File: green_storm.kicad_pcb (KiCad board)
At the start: 2 copper layers, 28 parts, among them J1 USB_B_Micro, J2 Conn_01x04, J3 Conn_01x04, J4 Conn_01x04, SW1 SW_SPDT, U1 AMS1117-3.3, U2 STM32F103C8T6, Y1 16Mhz

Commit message: Routing half-way complete
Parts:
- added H1: MountingHole, MountingHole:MountingHole_2.2mm_M2, F.Cu at (48.0, 105.0)
- added H2: MountingHole, MountingHole:MountingHole_2.2mm_M2, F.Cu at (89.9, 105.0)
- added H3: MountingHole, MountingHole:MountingHole_2.2mm_M2, F.Cu at (90.0, 80.0)
- added H4: MountingHole, MountingHole:MountingHole_2.2mm_M2, F.Cu at (48.0, 80.0)
- moved C3 98.8 mm to (64.6, 82.8)
- moved R4 91.2 mm to (64.4, 102.1), turned to 180 degrees
- moved R5 88.5 mm to (67.1, 102.1)
- moved U1 86.1 mm to (75.9, 102.7), turned to 180 degrees
- moved C1 85.5 mm to (78.4, 97.9)
- moved C2 82.5 mm to (81.5, 101.3), turned to 90 degrees
- moved J4 79.2 mm to (68.8, 110.2), turned to -90 degrees
- moved D1 78.7 mm to (84.8, 101.5), turned to 90 degrees
- moved R1 70.5 mm to (85.1, 98.3), turned to 90 degrees
- moved R2 10.3 mm to (59.8, 85.0), turned to 90 degrees
- moved J1 8.65 mm to (91.9, 89.8)
- moved SW1 7.13 mm to (44.4, 87.5), turned to -90 degrees
- moved J3 4.18 mm to (65.7, 76.1)
- moved J2 4.17 mm to (80.8, 76.1)
- moved R3 2.79 mm to (78.5, 89.4), turned to -90 degrees
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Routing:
- net Net-(J1-D-): track 0.00 -> 19.1 mm
- net Net-(J1-D+): track 0.00 -> 19.0 mm
- net Net-(J2-Pin_2): track 0.00 -> 18.4 mm
- net Net-(J3-Pin_3): track 0.00 -> 17.6 mm
- net Net-(J3-Pin_2): track 0.00 -> 17.1 mm
- net Net-(U2-BOOT0): track 0.00 -> 17.0 mm
- net +3.3V: track 0.00 -> 15.1 mm
- net GND: track 0.00 -> 14.7 mm
- net Net-(J2-Pin_3): track 0.00 -> 13.6 mm
- net Net-(U2-PD0): track 0.00 -> 8.73 mm
- net Net-(U2-PD1): track 0.00 -> 6.10 mm
- net +3.3VA: track 0.00 -> 2.13 mm
- added copper zone on B.Cu, net GND
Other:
- board outline added: 54 x 38 mm

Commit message: Power puddle dropped
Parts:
- moved R2 10.8 mm to (49.0, 84.5)
- moved J4 5.91 mm to (62.9, 110.4), turned to 90 degrees
- moved C2 1.91 mm to (81.4, 103.3)
- moved C5 1.20 mm to (70.6, 97.7)
- moved C1 1.15 mm to (77.2, 98.0)
- moved U1 1.09 mm to (76.3, 103.8), turned to -90 degrees
- moved R4 0.51 mm to (64.9, 102.1)
- moved R5 0.25 mm to (67.3, 102.1)
- turned C11 to -90 degrees
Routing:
- net Net-(J4-Pin_2): track 0.00 -> 16.6 mm
- net Net-(J4-Pin_3): track 0.00 -> 15.6 mm
- net Net-(U2-NRST): track 0.00 -> 12.1 mm
- net GND: track 14.7 -> 25.2 mm, vias 0 -> 14
- net Net-(U2-BOOT0): track 17.0 -> 25.5 mm
- net Net-(SW1-B): track 0.00 -> 6.25 mm
- net +3.3V: track 15.1 -> 13.6 mm
- added copper zone on F.Cu, net GND

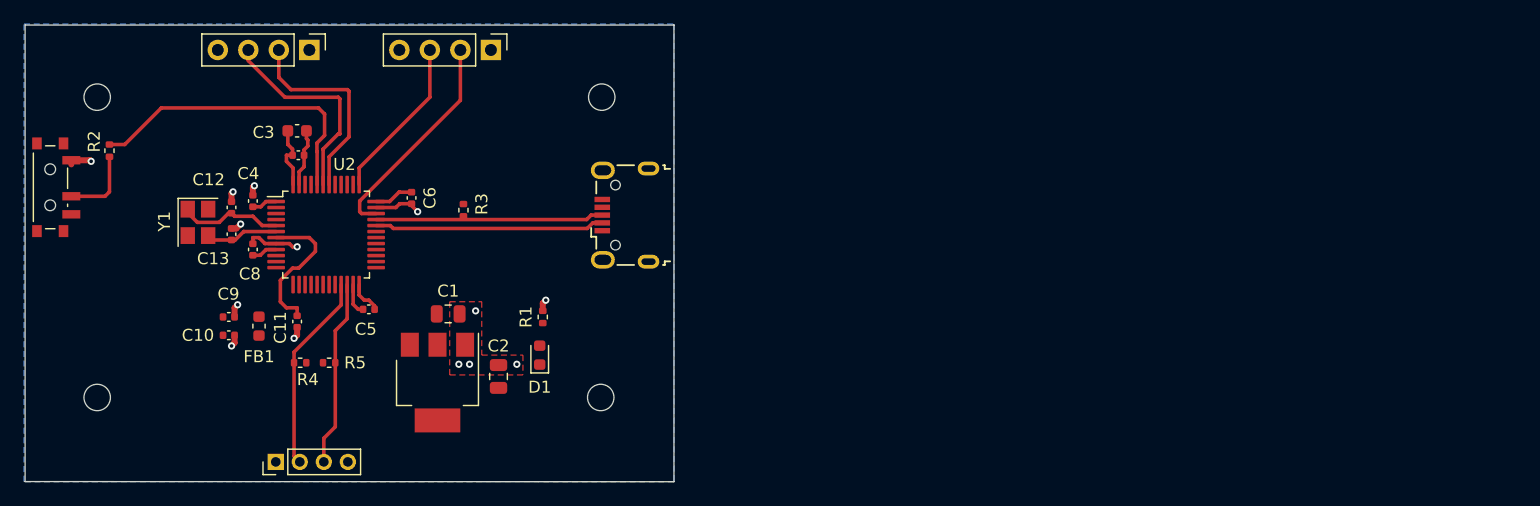
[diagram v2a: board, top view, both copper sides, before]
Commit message: Need error fixes on GND connections
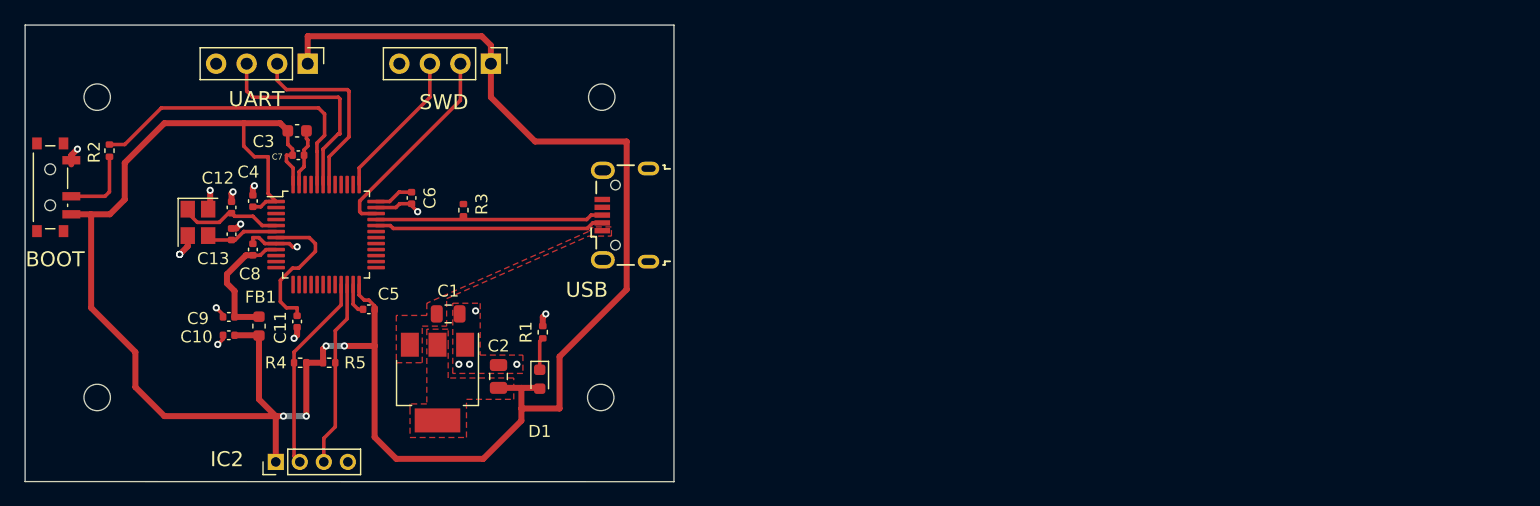
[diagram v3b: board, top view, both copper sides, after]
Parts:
- moved D1 2.01 mm to (84.8, 103.5), turned to -90 degrees
- moved R1 1.27 mm to (85.1, 99.6)
- moved J3 1.15 mm to (65.5, 77.2)
- moved J2 1.14 mm to (80.8, 77.2)
- turned C10 to 180 degrees
- turned C9 to 180 degrees
- turned FB1 to -90 degrees
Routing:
- net +3.3V: track 13.6 -> 194.6 mm, vias 0 -> 4
- net +3.3VA: track 2.13 -> 10.8 mm
- net GND: track 25.2 -> 27.9 mm, vias 14 -> 17
- net Net-(D1-K): track 0.00 -> 2.72 mm
- net Net-(J2-Pin_3): track 13.6 -> 12.5 mm
- net Net-(J2-Pin_2): track 18.4 -> 17.2 mm
- net Net-(J3-Pin_2): track 17.1 -> 16.2 mm
- removed copper zone on B.Cu, net GND
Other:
- board text added: "BOOT"
- board text added: "IC2"
- board text added: "SWD"
- board text added: "UART"
- board text added: "USB"

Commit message: Added ground plane, resolved GND vias issue
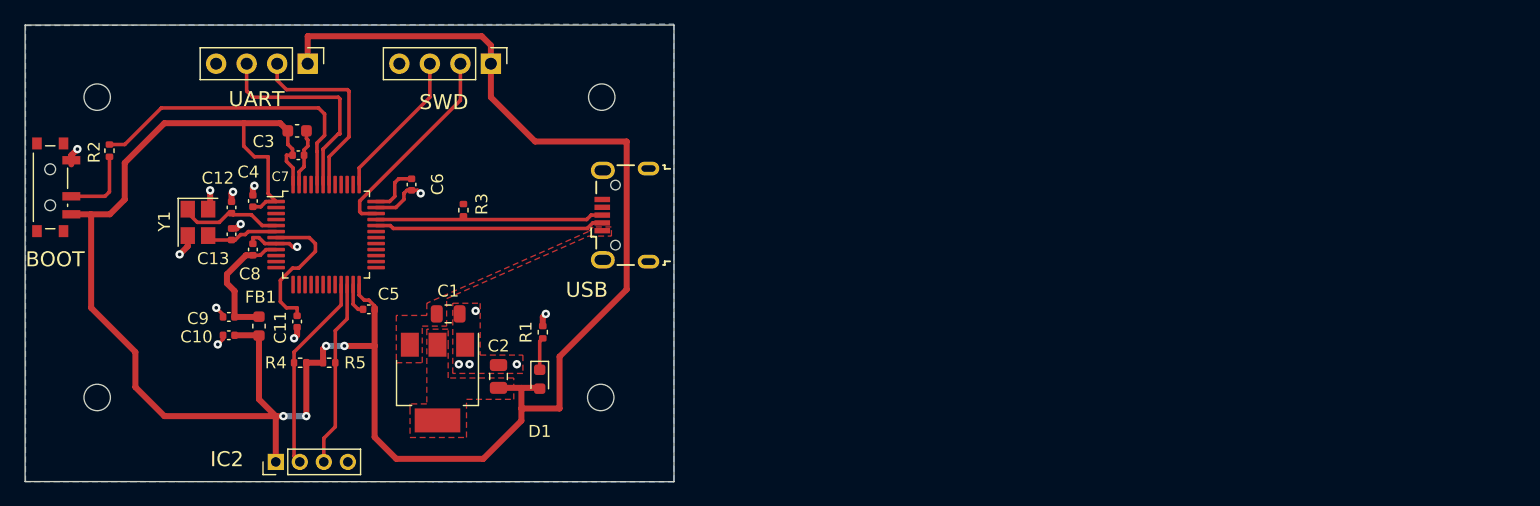
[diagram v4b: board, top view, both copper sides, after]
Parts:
- moved C6 1.11 mm to (74.2, 87.3)
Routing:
- net +3.3V: track 194.6 -> 195.7 mm
- net GND: track 27.9 -> 28.7 mm, vias 17 -> 16
- added copper zone on B.Cu, net GND

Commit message: Cleaned up more warnings
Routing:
- net GND: track 28.7 -> 29.8 mm, vias 16 -> 17
- added copper zone on F.Cu, net +3.3V
- added copper zone on F.Cu, net VBUS
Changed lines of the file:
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@@
   (segment (start 59.182 88.702) (end 59.182 88.011) (width 0.5) (layer "F.Cu") (net 2))
   (segment (start 65.222 84.836) (end 65.222 84.384) (width 0.3) (layer "F.Cu") (net 2))
+  (segment (start 89.408 88.519) (end 89.027 88.138) (width 0.3) (layer "F.Cu") (net 2))
   (segment (start 45.847 85.253) (end 46.01 85.253) (width 0.5) (layer "F.Cu") (net 2))
   (segment (start 61.964 92.19) (end 61.468 91.694) (width 0.3) (layer "F.Cu") (net 2))
@@
   (segment (start 55.538 92.417) (end 54.864 93.091) (width 0.5) (layer "F.Cu") (net 2))
   (segment (start 57.404 87.757) (end 57.404 89.158) (width 0.5) (layer "F.Cu") (net 2))
+  (segment (start 90.043 88.519) (end 89.408 88.519) (width 0.3) (layer "F.Cu") (net 2))
   (segment (start 58.476 98.1) (end 57.912 97.536) (width 0.3) (layer "F.Cu") (net 2))
   (segment (start 74.676 87.757) (end 74.93 88.011) (width 0.3) (layer "F.Cu") (net 2))
@@
   (via (at 54.864 93.091) (size 0.7) (drill 0.3) (layers "F.Cu" "B.Cu") (net 2))
   (via (at 85.344 98.044) (size 0.7) (drill 0.3) (layers "F.Cu" "B.Cu") (net 2))
+  (via (at 89.027 88.138) (size 0.7) (drill 0.3) (layers "F.Cu" "B.Cu") (net 2))
   (via (at 58.039 100.584) (size 0.7) (drill 0.3) (layers "F.Cu" "B.Cu") (net 2))
   (via (at 74.93 88.011) (size 0.7) (drill 0.3) (layers "F.Cu" "B.Cu") (net 2))
@@
   (segment (start 66.421 80.899) (end 53.34 80.899) (width 0.3) (layer "F.Cu") (net 20))
   (segment (start 66.306 84.539106) (end 66.294 84.527106) (width 0.3) (layer "F.Cu") (net 20))
-  (zone (net 2) (net_name "GND") (layer "F.Cu") (hatch edge 0.5)
+  (zone (net 1) (net_name "VBUS") (layer "F.Cu") (hatch edge 0.5)
     (priority 3)
     (connect_pads yes (clearance 0.3))
@@
     )
   )
-  (zone (net 2) (net_name "GND") (layer "F.Cu") (hatch edge 0.5)
+  (zone (net 3) (net_name "+3.3V") (layer "F.Cu") (hatch edge 0.5)
     (priority 2)
-    (connect_pads (clearance 0.3))
+    (connect_pads yes (clearance 0.3))
     (min_thickness 0.25) (filled_areas_thickness no)
     (fill yes (thermal_gap 0.5) (thermal_bridge_width 0.5))
@@
         (xy 74.041 108.331)
         (xy 78.74 108.331)
-        (xy 78.74 105.156)
-        (xy 82.677 105.156)
-        (xy 82.677 103.378)
+        (xy 78.74 105.537)
+        (xy 82.677 105.537)
+        (xy 82.677 103.251)
         (xy 77.216 103.378)
         (xy 77.216 100.711)
         (xy 77.216 99.314)
-        (xy 75.438 99.314)
-        (xy 75.438 105.537)
+        (xy 75.184 99.314)
+        (xy 75.184 105.537)
         (xy 74.041 105.537)
         (xy 74.041 105.918)

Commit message: Off to Manufacturing
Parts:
- added G***: LOGO, LOGO, F.Cu at (45.1, 101.0)
- J4: footprint Connector_PinHeader_2.00mm:PinHeader_1x04_P2.00mm_Vertical -> Connector_PinHeader_2.54mm:PinHeader_1x04_P2.54mm_Vertical
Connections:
- J1 pad 6: unconnected-(J1-Shield-Pad6) -> GND
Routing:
- net +3.3V: track 195.7 -> 209.3 mm
- net GND: track 29.8 -> 42.1 mm, vias 17 -> 24
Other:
- board text added: "Hotsauce Labs"
